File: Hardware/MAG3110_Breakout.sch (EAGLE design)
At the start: 18 parts, among them U1 MAG3110

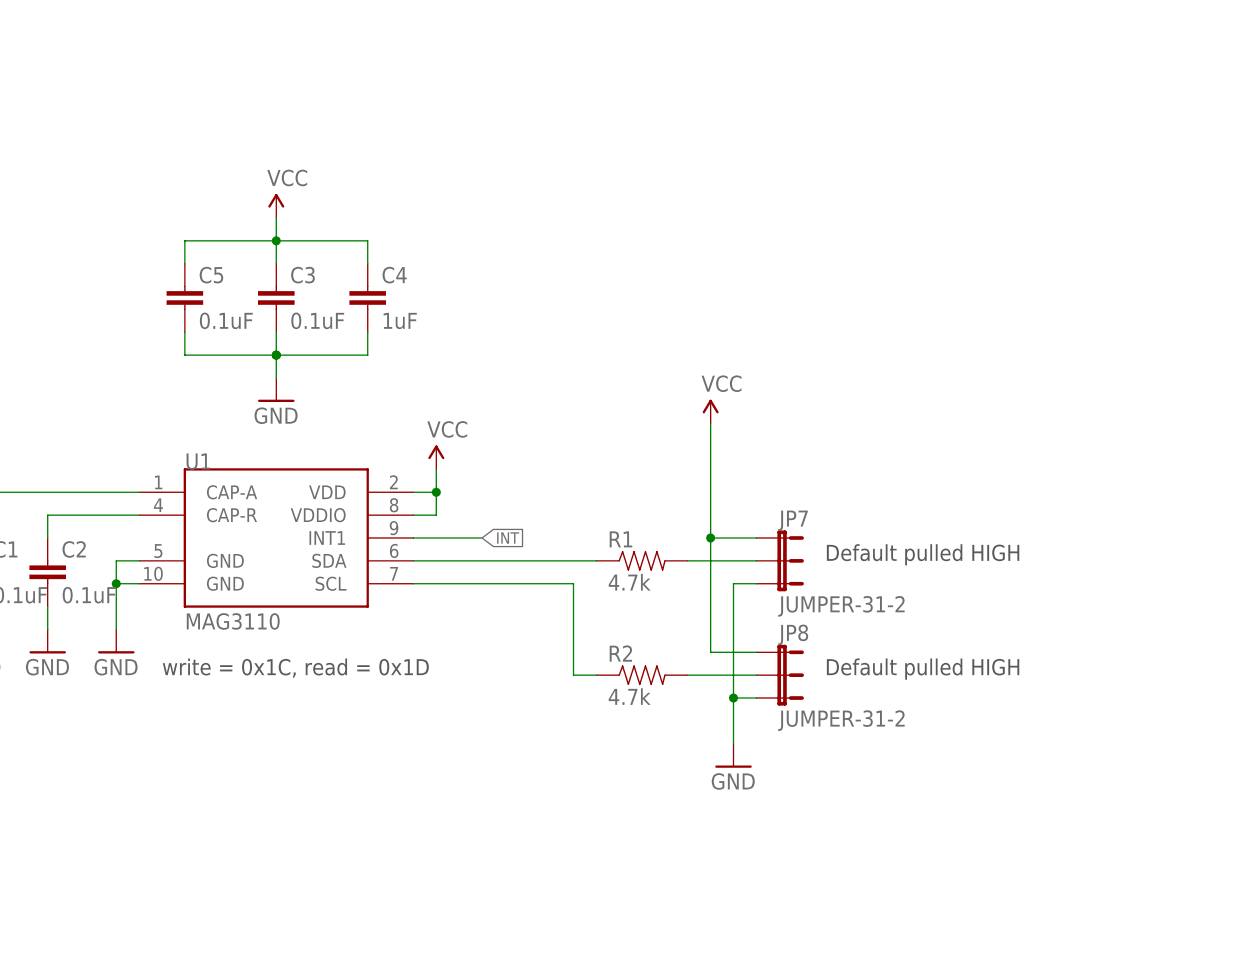
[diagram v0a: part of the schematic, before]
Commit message: Fixed pullup jumper and C3 position
Removed both three pad jumpers. Replaced with one jumper to pullup I2C
lines. Moved C3 closer to pin 8. Corrected 4 way VCC net in schematic.
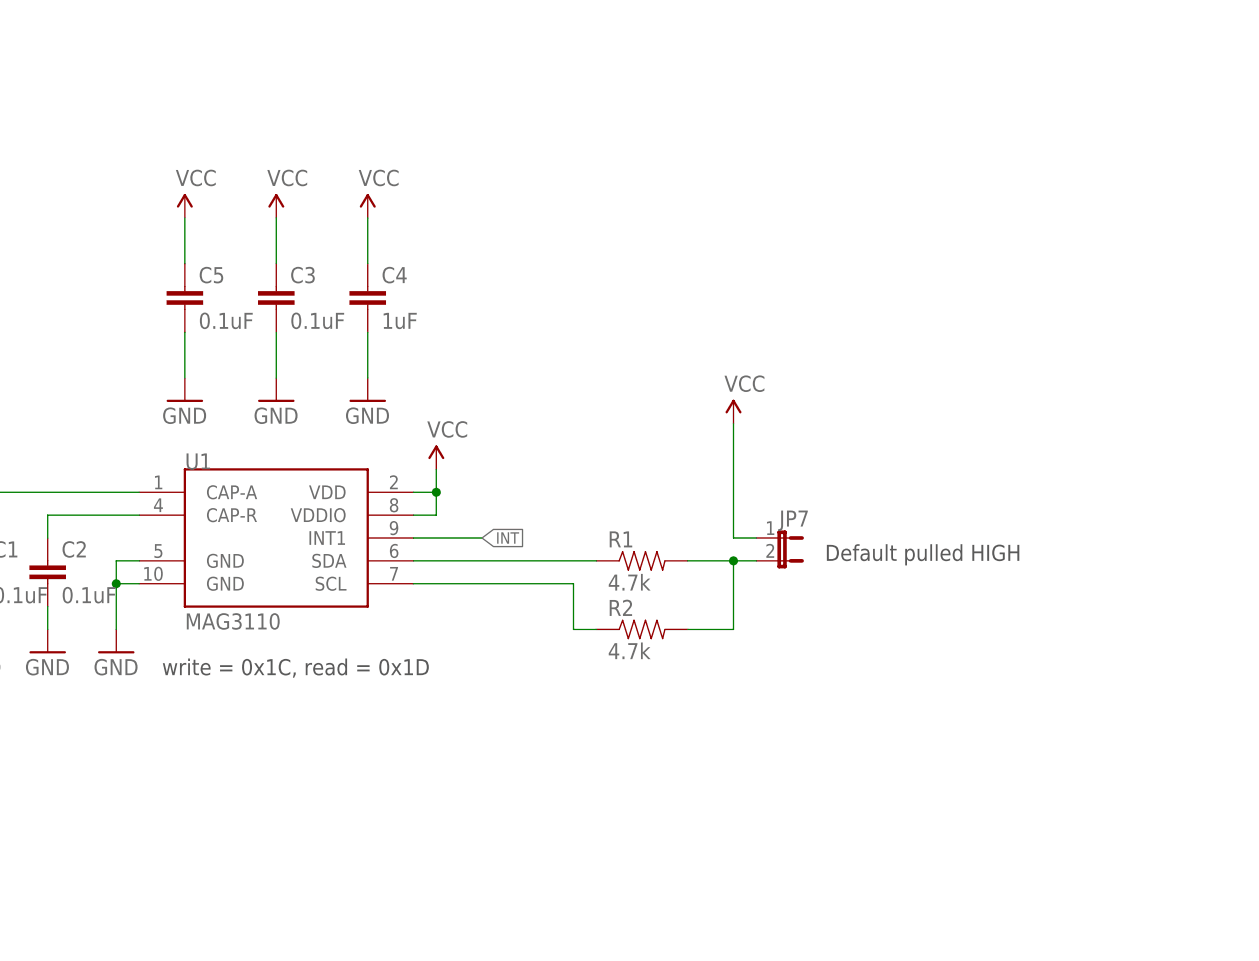
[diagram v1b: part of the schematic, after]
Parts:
- removed JP8: JUMPER-31-2, SparkFun-Passives:JUMPER-31-2
- JP7: value JUMPER-31-2 -> (none); device SparkFun-Passives:JUMPER-31-2 -> SparkFun-Passives:JUMPER-2SMD-NC
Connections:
- removed net N$4: JP7.2, R1.2
- net GND: no longer JP7.3, JP8.3
- net N$3: now also JP7.2, R1.2; no longer JP8.2
- net VCC: no longer JP8.1
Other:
- moved on the sheet: R2
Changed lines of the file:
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@@
 <?xml version="1.0" encoding="utf-8"?>
 <!DOCTYPE eagle SYSTEM "eagle.dtd">
-<eagle version="6.5.0">
+<eagle version="6.4">
 <drawing>
 <settings>
@@
 <part name="JP6" library="abes" deviceset="FIDUCIAL" device="1X2.5"/>
 <part name="FRAME2" library="SparkFun-Aesthetics" deviceset="FRAME-LETTER" device=""/>
-<part name="JP7" library="SparkFun-Passives" deviceset="JUMPER-3" device="1-2"/>
-<part name="JP8" library="SparkFun-Passives" deviceset="JUMPER-3" device="1-2"/>
-<part name="GND6" library="SparkFun" deviceset="GND" device=""/>
 <part name="LOGO1" library="SparkFun-Aesthetics" deviceset="OSHW-LOGO" device="S"/>
+<part name="P+5" library="SparkFun" deviceset="VCC" device=""/>
+<part name="P+6" library="SparkFun" deviceset="VCC" device=""/>
+<part name="GND7" library="SparkFun" deviceset="GND" device=""/>
+<part name="GND8" library="SparkFun" deviceset="GND" device=""/>
+<part name="JP7" library="SparkFun-Passives" deviceset="JUMPER-2" device="SMD-NC"/>
 </parts>
 <sheets>
@@
 <text x="167.64" y="10.16" size="2.54" layer="94" ratio="15">Kade Jensen</text>
 <text x="185.42" y="83.82" size="1.778" layer="97">Default pulled HIGH</text>
-<text x="185.42" y="71.12" size="1.778" layer="97">Default pulled HIGH</text>
 </plain>
 <instances>
@@
 <instance part="C5" gate="G$1" x="114.3" y="111.76"/>
 <instance part="R1" gate="G$1" x="165.1" y="83.82"/>
-<instance part="R2" gate="G$1" x="165.1" y="71.12"/>
-<instance part="P+3" gate="1" x="172.72" y="99.06"/>
+<instance part="R2" gate="G$1" x="165.1" y="76.2"/>
+<instance part="P+3" gate="1" x="175.26" y="99.06"/>
 <instance part="JP1" gate="G$1" x="68.58" y="111.76"/>
 <instance part="P+4" gate="1" x="78.74" y="119.38"/>
@@
 <instance part="FRAME2" gate="G$1" x="0" y="0"/>
 <instance part="FRAME2" gate="G$2" x="147.32" y="0"/>
-<instance part="JP7" gate="G$1" x="180.34" y="86.36" rot="R270"/>
-<instance part="JP8" gate="G$1" x="180.34" y="73.66" rot="R270"/>
-<instance part="GND6" gate="1" x="175.26" y="60.96"/>
 <instance part="LOGO1" gate="G$1" x="15.24" y="12.7"/>
+<instance part="P+5" gate="1" x="114.3" y="121.92"/>
+<instance part="P+6" gate="1" x="134.62" y="121.92"/>
+<instance part="GND7" gate="1" x="114.3" y="101.6"/>
+<instance part="GND8" gate="1" x="134.62" y="101.6"/>
+<instance part="JP7" gate="A" x="180.34" y="86.36" rot="R270"/>
 </instances>
 <busses>
@@
 </segment>
 <segment>
-<wire x1="124.46" y1="109.22" x2="124.46" y2="106.68" width="0.1524" layer="91"/>
-<wire x1="124.46" y1="106.68" x2="134.62" y2="106.68" width="0.1524" layer="91"/>
-<wire x1="134.62" y1="106.68" x2="134.62" y2="109.22" width="0.1524" layer="91"/>
-<wire x1="124.46" y1="104.14" x2="124.46" y2="106.68" width="0.1524" layer="91"/>
-<wire x1="124.46" y1="106.68" x2="114.3" y2="106.68" width="0.1524" layer="91"/>
-<wire x1="114.3" y1="106.68" x2="114.3" y2="109.22" width="0.1524" layer="91"/>
-<junction x="124.46" y="106.68"/>
-<junction x="124.46" y="106.68"/>
+<wire x1="124.46" y1="104.14" x2="124.46" y2="109.22" width="0.1524" layer="91"/>
 <pinref part="C3" gate="G$1" pin="2"/>
-<pinref part="C4" gate="G$1" pin="2"/>
 <pinref part="GND4" gate="1" pin="GND"/>
-<pinref part="C5" gate="G$1" pin="2"/>
 </segment>
 <segment>
@@
 </segment>
 <segment>
-<pinref part="JP7" gate="G$1" pin="3"/>
-<wire x1="177.8" y1="81.28" x2="175.26" y2="81.28" width="0.1524" layer="91"/>
-<wire x1="175.26" y1="81.28" x2="175.26" y2="68.58" width="0.1524" layer="91"/>
-<pinref part="JP8" gate="G$1" pin="3"/>
-<wire x1="175.26" y1="68.58" x2="175.26" y2="63.5" width="0.1524" layer="91"/>
-<wire x1="177.8" y1="68.58" x2="175.26" y2="68.58" width="0.1524" layer="91"/>
-<junction x="175.26" y="68.58"/>
-<pinref part="GND6" gate="1" pin="GND"/>
+<pinref part="C4" gate="G$1" pin="2"/>
+<pinref part="GND8" gate="1" pin="GND"/>
+<wire x1="134.62" y1="109.22" x2="134.62" y2="104.14" width="0.1524" layer="91"/>
+</segment>
+<segment>
+<pinref part="C5" gate="G$1" pin="2"/>
+<pinref part="GND7" gate="1" pin="GND"/>
+<wire x1="114.3" y1="109.22" x2="114.3" y2="104.14" width="0.1524" layer="91"/>
 </segment>
 </net>
 <net name="VCC" class="0">
 <segment>
-<wire x1="124.46" y1="116.84" x2="124.46" y2="119.38" width="0.1524" layer="91"/>
-<wire x1="124.46" y1="119.38" x2="134.62" y2="119.38" width="0.1524" layer="91"/>
-<wire x1="134.62" y1="119.38" x2="134.62" y2="116.84" width="0.1524" layer="91"/>
-<wire x1="124.46" y1="121.92" x2="124.46" y2="119.38" width="0.1524" layer="91"/>
-<wire x1="114.3" y1="116.84" x2="114.3" y2="119.38" width="0.1524" layer="91"/>
-<wire x1="114.3" y1="119.38" x2="124.46" y2="119.38" width="0.1524" layer="91"/>
-<junction x="124.46" y="119.38"/>
+<wire x1="124.46" y1="121.92" x2="124.46" y2="116.84" width="0.1524" layer="91"/>
 <pinref part="C3" gate="G$1" pin="1"/>
-<pinref part="C4" gate="G$1" pin="1"/>
 <pinref part="P+1" gate="1" pin="VCC"/>
-<pinref part="C5" gate="G$1" pin="1"/>
 </segment>
 <segment>
@@
 </segment>
 <segment>
-<pinref part="JP7" gate="G$1" pin="1"/>
 <pinref part="P+3" gate="1" pin="VCC"/>
-<wire x1="177.8" y1="86.36" x2="172.72" y2="86.36" width="0.1524" layer="91"/>
-<wire x1="172.72" y1="86.36" x2="172.72" y2="99.06" width="0.1524" layer="91"/>
-<pinref part="JP8" gate="G$1" pin="1"/>
-<wire x1="177.8" y1="73.66" x2="172.72" y2="73.66" width="0.1524" layer="91"/>
-<wire x1="172.72" y1="73.66" x2="172.72" y2="86.36" width="0.1524" layer="91"/>
-<junction x="172.72" y="86.36"/>
+<wire x1="175.26" y1="86.36" x2="175.26" y2="99.06" width="0.1524" layer="91"/>
+<pinref part="JP7" gate="A" pin="1"/>
+<wire x1="177.8" y1="86.36" x2="175.26" y2="86.36" width="0.1524" layer="91"/>
+</segment>
+<segment>
+<pinref part="C5" gate="G$1" pin="1"/>
+<pinref part="P+5" gate="1" pin="VCC"/>
+<wire x1="114.3" y1="116.84" x2="114.3" y2="121.92" width="0.1524" layer="91"/>
+</segment>
+<segment>
+<pinref part="C4" gate="G$1" pin="1"/>
+<pinref part="P+6" gate="1" pin="VCC"/>
+<wire x1="134.62" y1="121.92" x2="134.62" y2="116.84" width="0.1524" layer="91"/>
 </segment>
 </net>
@@
 <net name="SCL" class="0">
 <segment>
-<wire x1="157.48" y1="71.12" x2="160.02" y2="71.12" width="0.1524" layer="91"/>
+<wire x1="157.48" y1="76.2" x2="160.02" y2="76.2" width="0.1524" layer="91"/>
 <pinref part="R2" gate="G$1" pin="1"/>
 <pinref part="U1" gate="G$1" pin="SCL"/>
 <wire x1="139.7" y1="81.28" x2="157.48" y2="81.28" width="0.1524" layer="91"/>
-<wire x1="157.48" y1="81.28" x2="157.48" y2="71.12" width="0.1524" layer="91"/>
+<wire x1="157.48" y1="81.28" x2="157.48" y2="76.2" width="0.1524" layer="91"/>
 </segment>
 <segment>
@@
 <segment>
 <pinref part="R2" gate="G$1" pin="2"/>
-<pinref part="JP8" gate="G$1" pin="2"/>
-<wire x1="170.18" y1="71.12" x2="177.8" y2="71.12" width="0.1524" layer="91"/>
-</segment>
-</net>
-<net name="N$4" class="0">
-<segment>
+<wire x1="170.18" y1="76.2" x2="175.26" y2="76.2" width="0.1524" layer="91"/>
 <pinref part="R1" gate="G$1" pin="2"/>
-<pinref part="JP7" gate="G$1" pin="2"/>
-<wire x1="170.18" y1="83.82" x2="177.8" y2="83.82" width="0.1524" layer="91"/>
-</segment>
-</net>
+<wire x1="170.18" y1="83.82" x2="175.26" y2="83.82" width="0.1524" layer="91"/>
+<pinref part="JP7" gate="A" pin="2"/>
+<wire x1="175.26" y1="83.82" x2="177.8" y2="83.82" width="0.1524" layer="91"/>
+<wire x1="175.26" y1="76.2" x2="175.26" y2="83.82" width="0.1524" layer="91"/>
+<junction x="175.26" y="83.82"/>
+</segment>
+</net>

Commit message: Updated main IC to 1:1
Updated footprint on main IC to 1:1 for better reflow and AOI.
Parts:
- U1: value MAG3110 -> MAG31101:1; device SparkFun:MAG3110 -> SparkFun-Sensors:MAG31101:1
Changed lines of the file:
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@@
 </classes>
 <parts>
-<part name="U1" library="SparkFun" deviceset="MAG3110" device=""/>
+<part name="U1" library="SparkFun-Sensors" deviceset="MAG3110" device="1:1"/>
 <part name="C1" library="SparkFun" deviceset="CAP" device="0603-CAP" value="0.1uF"/>
 <part name="C2" library="SparkFun" deviceset="CAP" device="0603-CAP" value="0.1uF"/>
